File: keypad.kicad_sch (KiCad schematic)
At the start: 3 parts

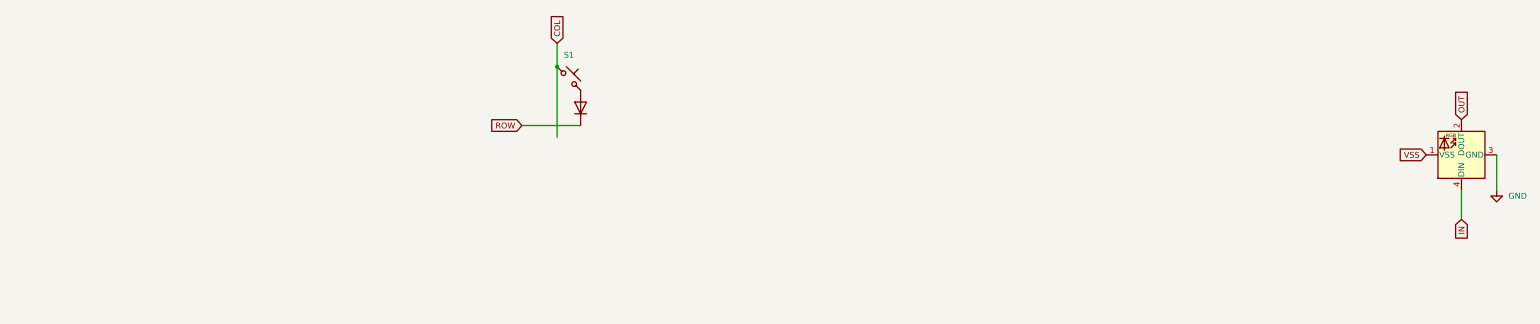
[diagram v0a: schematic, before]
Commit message: Adding choc v2 support and VCC denoise cap
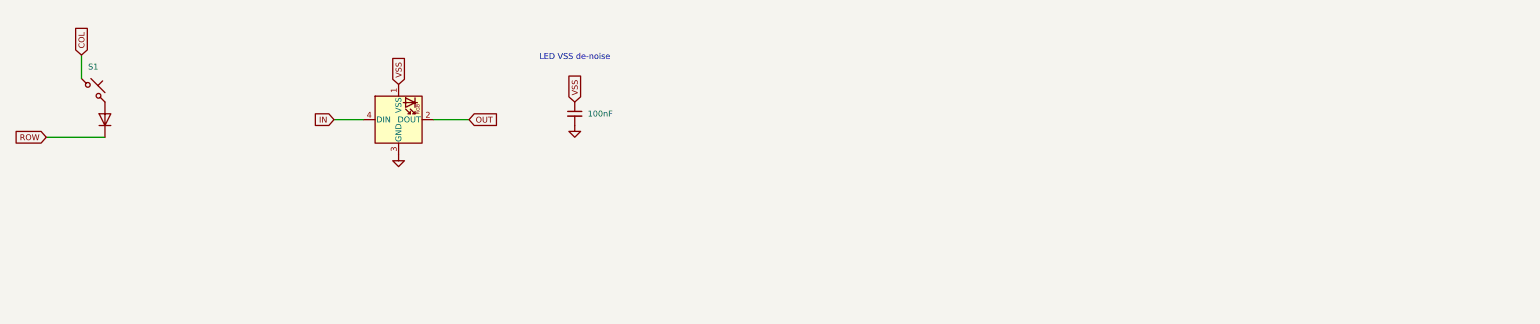
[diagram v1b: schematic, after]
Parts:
- added C1: 100nF, Capacitor_SMD:C_0603_1608Metric, symbol Device:C_Small
- D1: footprint ScottoKeebs_Components:Diode_SOD-123 -> Diode_SMD:D_SOD-523
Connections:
- net GND: now also C1.2
- net VSS: now also C1.1
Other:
- note added: "LED VSS de-noise"
- moved on the sheet: S1

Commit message: BOM patches
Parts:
- C1: LCSC C1525 -> C14663
- D1: LCSC (none) -> C83482
- D2: LCSC (none) -> C5149201
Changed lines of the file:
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@@
+			)
+		)
+		(property "LCSC" "C83482"
+			(at 55.88 49.53 90)
+			(effects
+				(font
+					(size 1.27 1.27)
+				)
+				(hide yes)
 			)
 		)
@@
 			)
 		)
-		(property "LCSC" "C1525"
+		(property "LCSC" "C14663"
 			(at 157.48 48.26 0)
 			(effects
@@
 			(effects
 				(font
+					(size 1.27 1.27)
+				)
+				(hide yes)
+			)
+		)
+		(property "LCSC" "C5149201"
+			(at 119.38 49.53 90)
+			(effects
+				(font

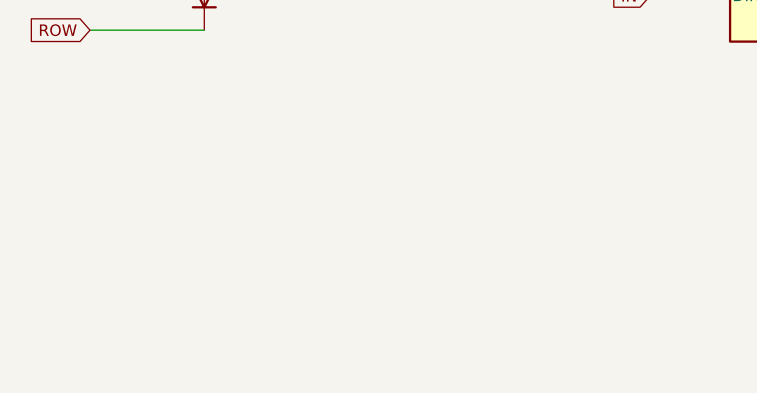
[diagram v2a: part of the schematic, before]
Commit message: Swapping the socket model
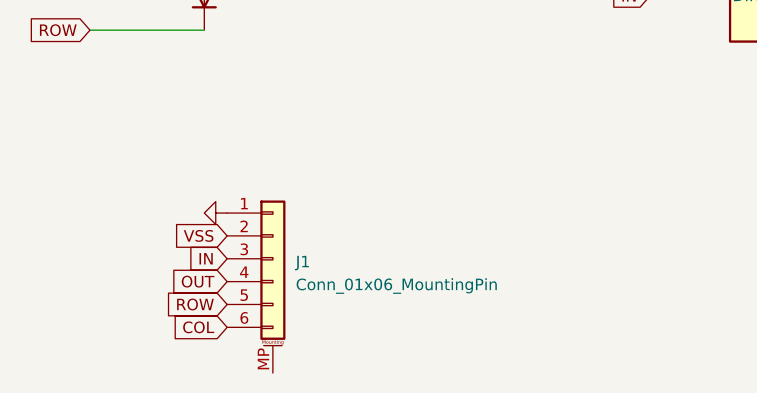
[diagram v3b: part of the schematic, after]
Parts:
- added J1: Conn_01x06_MountingPin, Hirose_FH19C-6S-0.5SH_1x06:Hirose_FH19C-6S-0.5SH_1x06, symbol Connector_Generic_MountingPin:Conn_01x06_MountingPin
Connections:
- net COL: now also J1.6 (Pin_6)
- net GND: now also J1.1 (Pin_1)
- net IN: now also J1.3 (Pin_3)
- net OUT: now also J1.4 (Pin_4)
- net ROW: now also J1.5 (Pin_5)
- net VSS: now also J1.2 (Pin_2)
